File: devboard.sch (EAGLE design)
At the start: 40 parts, among them IC1 ATMEGA1284, Q1 CRYSTALX22, X1 MICROMATCH-8

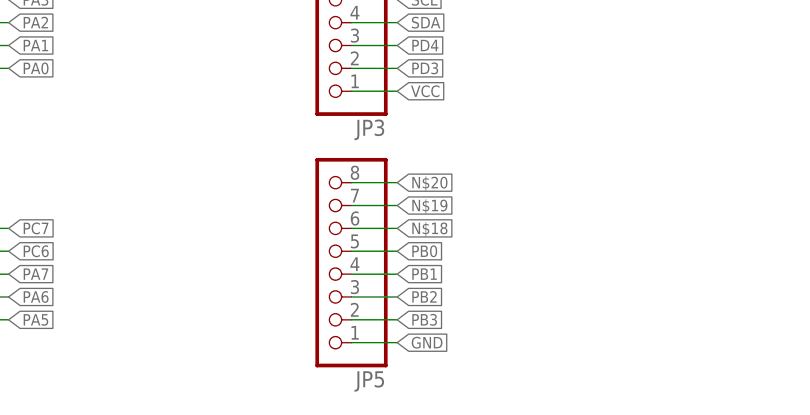
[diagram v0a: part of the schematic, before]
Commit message: updated to include MISO,MOSI,SCLK to external pins
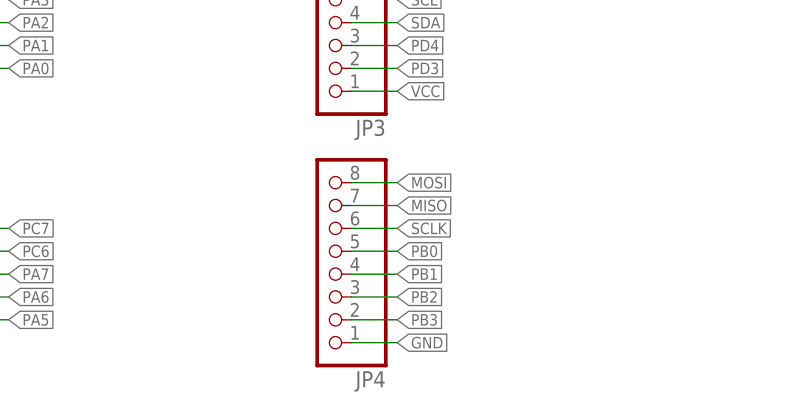
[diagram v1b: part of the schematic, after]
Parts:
- renumbered JP5 to JP4
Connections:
- removed net N$18: JP4.6
- removed net N$19: JP4.7
- removed net N$20: JP4.8
- net MISO: now also JP4.7
- net MOSI: now also JP4.8
- net SCLK: now also JP4.6
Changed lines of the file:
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@@
 <part name="R26" library="rcl" deviceset="R-EU_" device="R0603" value="0R"/>
 <part name="U$1" library="artwork" deviceset="HEXAKRAKE" device=""/>
-<part name="JP5" library="pinhead" deviceset="PINHD-1X8" device=""/>
+<part name="JP4" library="pinhead" deviceset="PINHD-1X8" device=""/>
 </parts>
 <sheets>
@@
 <instance part="R26" gate="G$1" x="200.66" y="43.18" rot="R90"/>
 <instance part="U$1" gate="G$1" x="111.76" y="22.86"/>
-<instance part="JP5" gate="A" x="55.88" y="20.32" rot="R180"/>
+<instance part="JP4" gate="A" x="55.88" y="20.32" rot="R180"/>
 </instances>
 <busses>
@@
 </segment>
 <segment>
-<pinref part="JP5" gate="A" pin="1"/>
+<pinref part="JP4" gate="A" pin="1"/>
 <wire x1="58.42" y1="10.16" x2="63.5" y2="10.16" width="0.1524" layer="91"/>
 <label x="63.5" y="10.16" size="1.27" layer="95" xref="yes"/>
@@
 <pinref part="IC1" gate="G$1" pin="(PCINT14/MISO)PB6"/>
 </segment>
+<segment>
+<pinref part="JP4" gate="A" pin="7"/>
+<wire x1="58.42" y1="25.4" x2="63.5" y2="25.4" width="0.1524" layer="91"/>
+<label x="63.5" y="25.4" size="1.27" layer="95" xref="yes"/>
+</segment>
 </net>
 <net name="MOSI" class="0">
@@
 <label x="246.38" y="139.7" size="1.27" layer="95" xref="yes"/>
 <pinref part="IC1" gate="G$1" pin="(PCINT13/MOSI)PB5"/>
+</segment>
+<segment>
+<pinref part="JP4" gate="A" pin="8"/>
+<wire x1="58.42" y1="27.94" x2="63.5" y2="27.94" width="0.1524" layer="91"/>
+<label x="63.5" y="27.94" size="1.27" layer="95" xref="yes"/>
 </segment>
 </net>
@@
 </segment>
 <segment>
-<pinref part="JP5" gate="A" pin="5"/>
+<pinref part="JP4" gate="A" pin="5"/>
 <wire x1="58.42" y1="20.32" x2="63.5" y2="20.32" width="0.1524" layer="91"/>
 <label x="63.5" y="20.32" size="1.27" layer="95" xref="yes"/>
@@
 </segment>
 <segment>
-<pinref part="JP5" gate="A" pin="4"/>
+<pinref part="JP4" gate="A" pin="4"/>
 <wire x1="58.42" y1="17.78" x2="63.5" y2="17.78" width="0.1524" layer="91"/>
 <label x="63.5" y="17.78" size="1.27" layer="95" xref="yes"/>
@@
 </segment>
 <segment>
-<pinref part="JP5" gate="A" pin="3"/>
+<pinref part="JP4" gate="A" pin="3"/>
 <wire x1="58.42" y1="15.24" x2="63.5" y2="15.24" width="0.1524" layer="91"/>
 <label x="63.5" y="15.24" size="1.27" layer="95" xref="yes"/>
@@
 </segment>
 <segment>
-<pinref part="JP5" gate="A" pin="2"/>
+<pinref part="JP4" gate="A" pin="2"/>
 <wire x1="58.42" y1="12.7" x2="63.5" y2="12.7" width="0.1524" layer="91"/>
 <label x="63.5" y="12.7" size="1.27" layer="95" xref="yes"/>
@@
 <label x="48.26" y="106.68" size="1.27" layer="95" rot="R180" xref="yes"/>
 <pinref part="U1" gate="G$1" pin="SCLK"/>
+</segment>
+<segment>
+<pinref part="JP4" gate="A" pin="6"/>
+<wire x1="58.42" y1="22.86" x2="63.5" y2="22.86" width="0.1524" layer="91"/>
+<label x="63.5" y="22.86" size="1.27" layer="95" xref="yes"/>
 </segment>
 </net>
@@
 </segment>
 </net>
-<net name="N$18" class="0">
-<segment>
-<pinref part="JP5" gate="A" pin="6"/>
-<wire x1="58.42" y1="22.86" x2="63.5" y2="22.86" width="0.1524" layer="91"/>
-<label x="63.5" y="22.86" size="1.27" layer="95" xref="yes"/>
-</segment>
-</net>
-<net name="N$19" class="0">
-<segment>
-<pinref part="JP5" gate="A" pin="7"/>
-<wire x1="58.42" y1="25.4" x2="63.5" y2="25.4" width="0.1524" layer="91"/>
-<label x="63.5" y="25.4" size="1.27" layer="95" xref="yes"/>
-</segment>
-</net>
-<net name="N$20" class="0">
-<segment>
-<pinref part="JP5" gate="A" pin="8"/>
-<wire x1="58.42" y1="27.94" x2="63.5" y2="27.94" width="0.1524" layer="91"/>
-<label x="63.5" y="27.94" size="1.27" layer="95" xref="yes"/>
-</segment>
-</net>

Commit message: changed C13, C14 to 0603
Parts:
- C13, C14: device rcl:C-EUC0805 -> rcl:C-EUC0603
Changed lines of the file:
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@@
 <parts>
 <part name="FRAME1" library="frames" deviceset="A4L-LOC" device=""/>
-<part name="C13" library="rcl" deviceset="C-EU" device="C0805" value="220nF"/>
+<part name="C13" library="rcl" deviceset="C-EU" device="C0603" value="220nF"/>
 <part name="C2" library="rcl" deviceset="C-EU" device="C0603" value="1uF"/>
 <part name="C3" library="rcl" deviceset="C-EU" device="C0603" value="1uF"/>
-<part name="C14" library="rcl" deviceset="C-EU" device="C0805" value="100nF"/>
+<part name="C14" library="rcl" deviceset="C-EU" device="C0603" value="100nF"/>
 <part name="C5" library="rcl" deviceset="C-EU" device="C0603" value="1uF"/>
 <part name="C6" library="rcl" deviceset="C-EU" device="C0603" value="1uF"/>

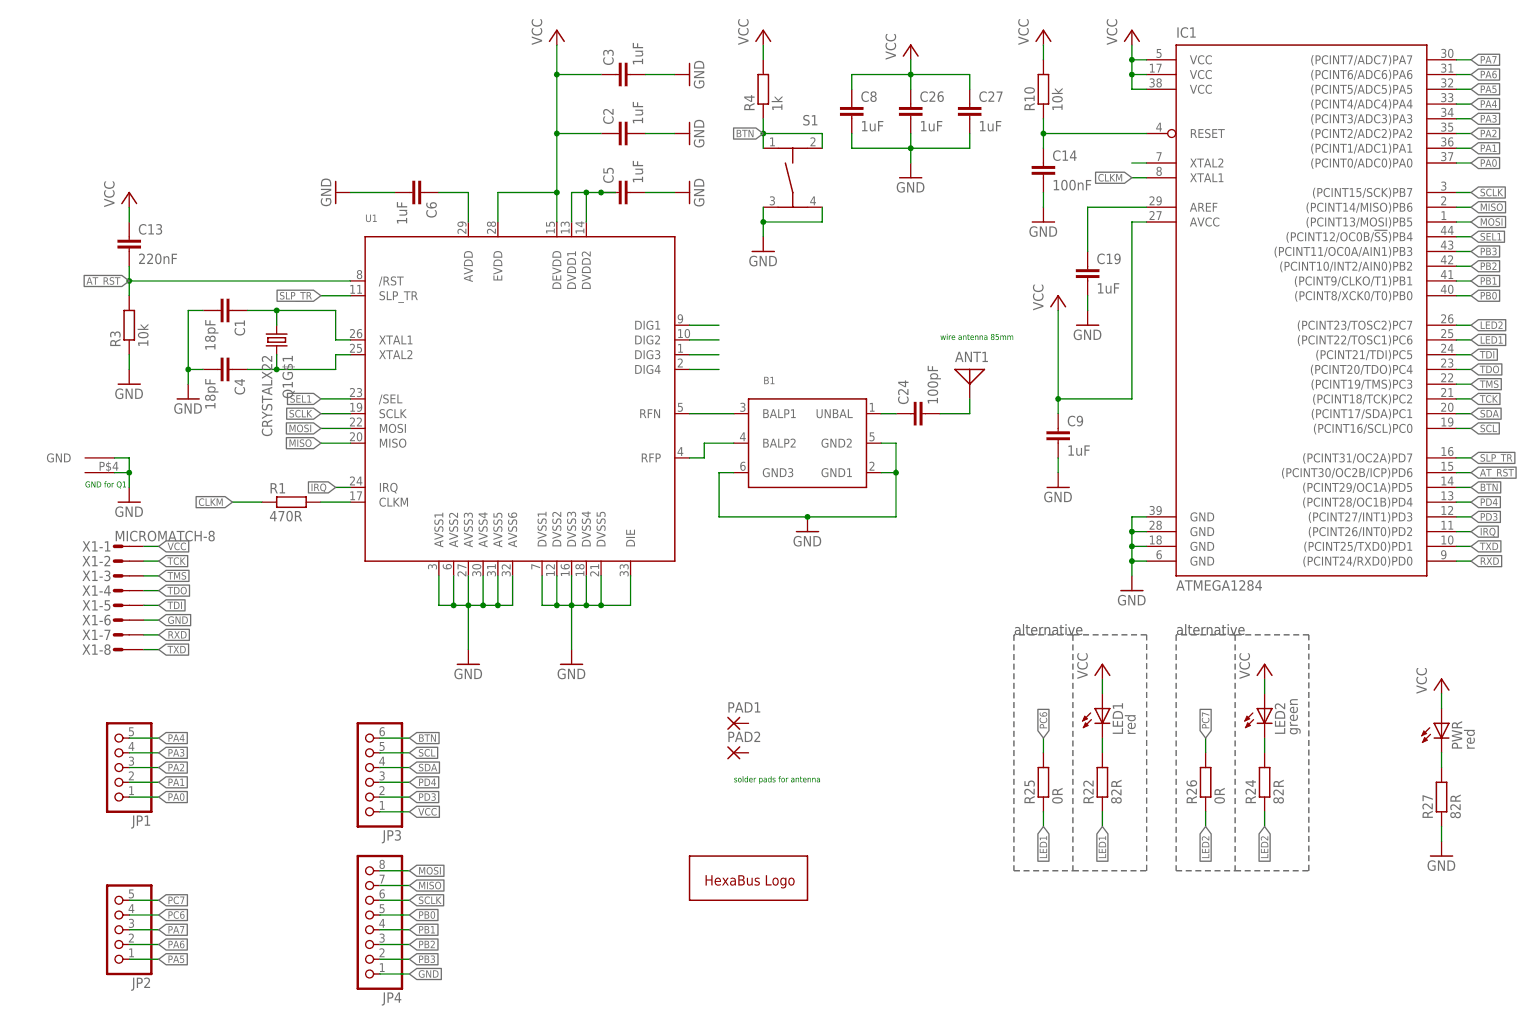
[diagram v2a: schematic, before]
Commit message: changed atmega to nonambiguous package
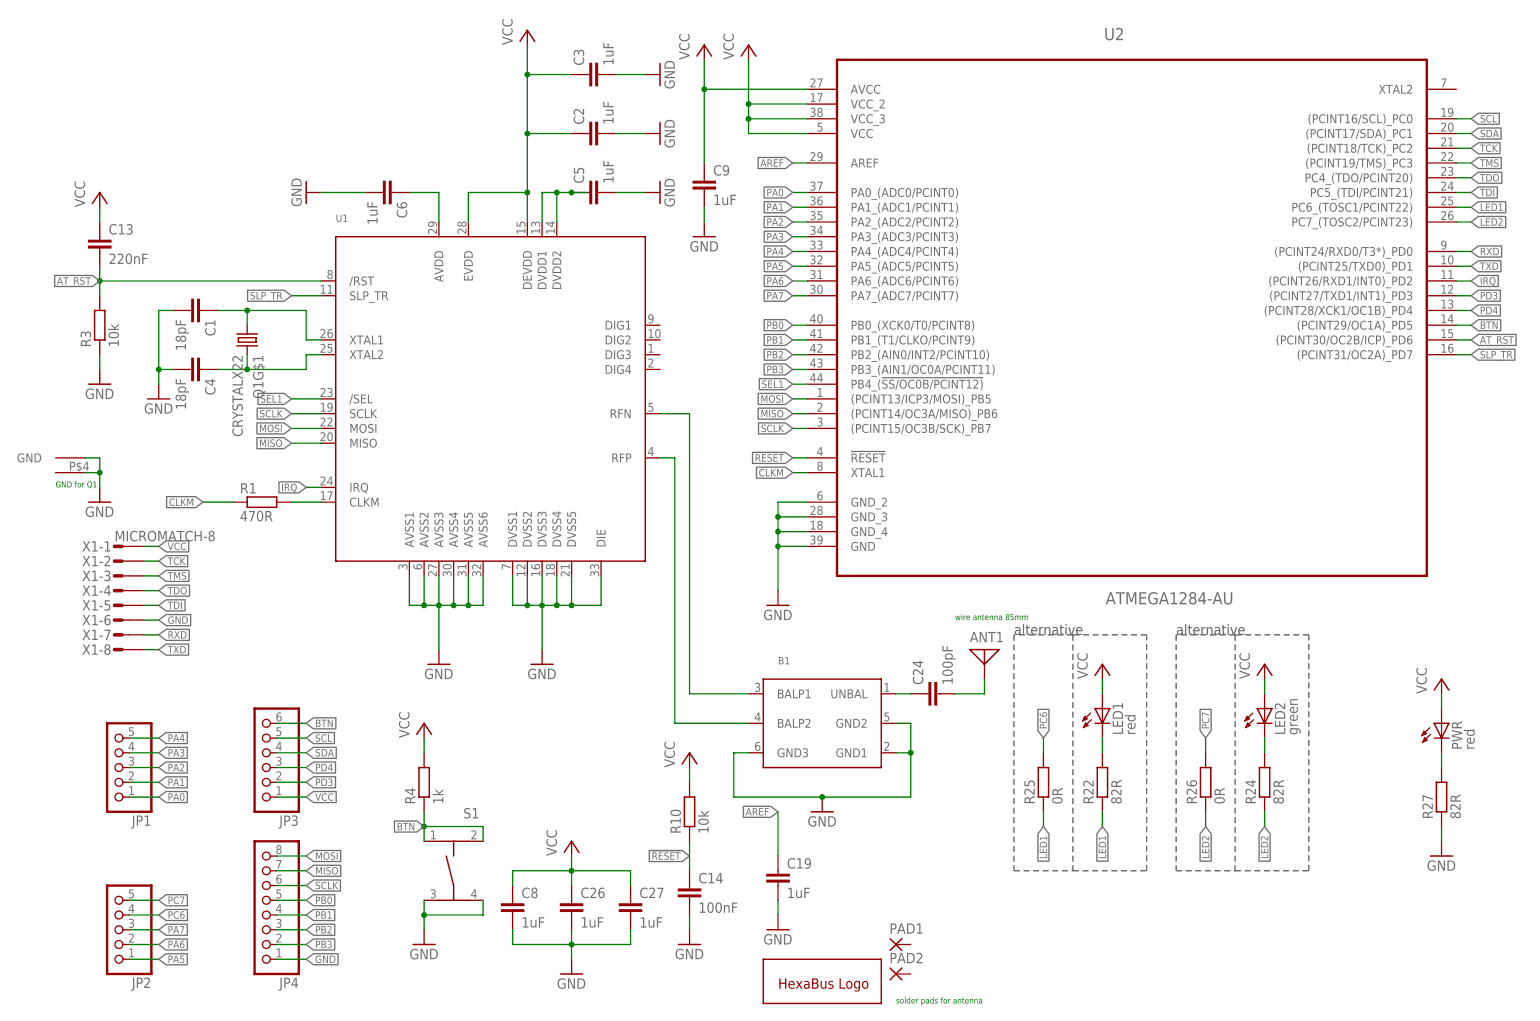
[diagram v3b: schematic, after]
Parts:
- removed IC1: ATMEGA1284, atmel:ATMEGA644A
- added U2: ATMEGA1284-AU, hexabus:ATMEGA1284-AU
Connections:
- removed net N$10: C19.1, IC1.AREF
- removed net N$11: C14.1, IC1.RESET, R10.1
- removed net N$12: IC1.XTAL2
- removed net N$3: U1.DIG1
- removed net N$6: U1.DIG2
- removed net N$7: U1.DIG3
- removed net N$8: U1.DIG4
- new net !RESET: C14.1, R10.1, U2.!RESET
- new net AREF: C19.1, U2.AREF
- net AT_RST: now also U2.(PCINT30/OC2B/ICP)_PD6; no longer IC1.(PCINT30/OC2B/ICP)PD6
- net BTN: now also U2.(PCINT29/OC1A)_PD5; no longer IC1.(PCINT29/OC1A)PD5
- net CLKM: now also U2.XTAL1; no longer IC1.XTAL1
- net GND: now also U2.GND, U2.GND_2, U2.GND_3, U2.GND_4; no longer IC1.GND, IC1.GND@1, IC1.GND@2, IC1.GND@3
- net IRQ: now also U2.(PCINT26/RXD1/INT0)_PD2; no longer IC1.(PCINT26/INT0)PD2
- net LED1: now also U2.PC6_(TOSC1/PCINT22); no longer IC1.(PCINT22/TOSC1)PC6
- net LED2: now also U2.PC7_(TOSC2/PCINT23); no longer IC1.(PCINT23/TOSC2)PC7
- net MISO: now also U2.(PCINT14/OC3A/MISO)_PB6; no longer IC1.(PCINT14/MISO)PB6
- net MOSI: now also U2.(PCINT13/ICP3/MOSI)_PB5; no longer IC1.(PCINT13/MOSI)PB5
- net PA0: now also U2.PA0_(ADC0/PCINT0); no longer IC1.(PCINT0/ADC0)PA0
- net PA1: now also U2.PA1_(ADC1/PCINT1); no longer IC1.(PCINT1/ADC1)PA1
- net PA2: now also U2.PA2_(ADC2/PCINT2); no longer IC1.(PCINT2/ADC2)PA2
- net PA3: now also U2.PA3_(ADC3/PCINT3); no longer IC1.(PCINT3/ADC3)PA3
- net PA4: now also U2.PA4_(ADC4/PCINT4); no longer IC1.(PCINT4/ADC4)PA4
- net PA5: now also U2.PA5_(ADC5/PCINT5); no longer IC1.(PCINT5/ADC5)PA5
- net PA6: now also U2.PA6_(ADC6/PCINT6); no longer IC1.(PCINT6/ADC6)PA6
- net PA7: now also U2.PA7_(ADC7/PCINT7); no longer IC1.(PCINT7/ADC7)PA7
- net PB0: now also U2.PB0_(XCK0/T0/PCINT8); no longer IC1.(PCINT8/XCK0/T0)PB0
- net PB1: now also U2.PB1_(T1/CLKO/PCINT9); no longer IC1.(PCINT9/CLKO/T1)PB1
- net PB2: now also U2.PB2_(AIN0/INT2/PCINT10); no longer IC1.(PCINT10/INT2/AIN0)PB2
- net PB3: now also U2.PB3_(AIN1/OC0A/PCINT11); no longer IC1.(PCINT11/OC0A/AIN1)PB3
- net PD3: now also U2.(PCINT27/TXD1/INT1)_PD3; no longer IC1.(PCINT27/INT1)PD3
- net PD4: now also U2.(PCINT28/XCK1/OC1B)_PD4; no longer IC1.(PCINT28/OC1B)PD4
- net RXD: now also U2.(PCINT24/RXD0/T3*)_PD0; no longer IC1.(PCINT24/RXD0)PD0
- net SCL: now also U2.(PCINT16/SCL)_PC0; no longer IC1.(PCINT16/SCL)PC0
- net SCLK: now also U2.(PCINT15/OC3B/SCK)_PB7; no longer IC1.(PCINT15/SCK)PB7
- net SDA: now also U2.(PCINT17/SDA)_PC1; no longer IC1.(PCINT17/SDA)PC1
- net SEL1: now also U2.PB4_(!SS/OC0B/PCINT12); no longer IC1.(PCINT12/OC0B/!SS!)PB4
- net SLP_TR: now also U2.(PCINT31/OC2A)_PD7; no longer IC1.(PCINT31/OC2A)PD7
- net TCK: now also U2.(PCINT18/TCK)_PC2; no longer IC1.(PCINT18/TCK)PC2
- net TDI: now also U2.PC5_(TDI/PCINT21); no longer IC1.(PCINT21/TDI)PC5
- net TDO: now also U2.PC4_(TDO/PCINT20); no longer IC1.(PCINT20/TDO)PC4
- net TMS: now also U2.(PCINT19/TMS)_PC3; no longer IC1.(PCINT19/TMS)PC3
- net TXD: now also U2.(PCINT25/TXD0)_PD1; no longer IC1.(PCINT25/TXD0)PD1
- net VCC: now also U2.AVCC, U2.VCC, U2.VCC_2, U2.VCC_3; no longer IC1.AVCC, IC1.VCC, IC1.VCC@1, IC1.VCC@2
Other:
- moved on the sheet: ANT1, B1, C1, C13, C14, C19, C2, C24, C26, C27, C3, C4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

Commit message: added note for  C1, C4
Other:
- note added: "do not populate C1, C4!"
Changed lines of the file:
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@@
 <text x="167.64" y="68.58" size="1.778" layer="97">alternative</text>
 <text x="195.58" y="68.58" size="1.778" layer="97">alternative</text>
+<text x="20.32" y="132.08" size="1.778" layer="97">do not populate C1, C4!</text>
 </plain>
 <instances>
